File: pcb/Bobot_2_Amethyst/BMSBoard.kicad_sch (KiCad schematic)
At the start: 5 parts, among them J3 Conn_01x05_Socket, J4 Conn_01x04_Socket, J7 Conn_01x02_Pin, U1 BQ25895RTW

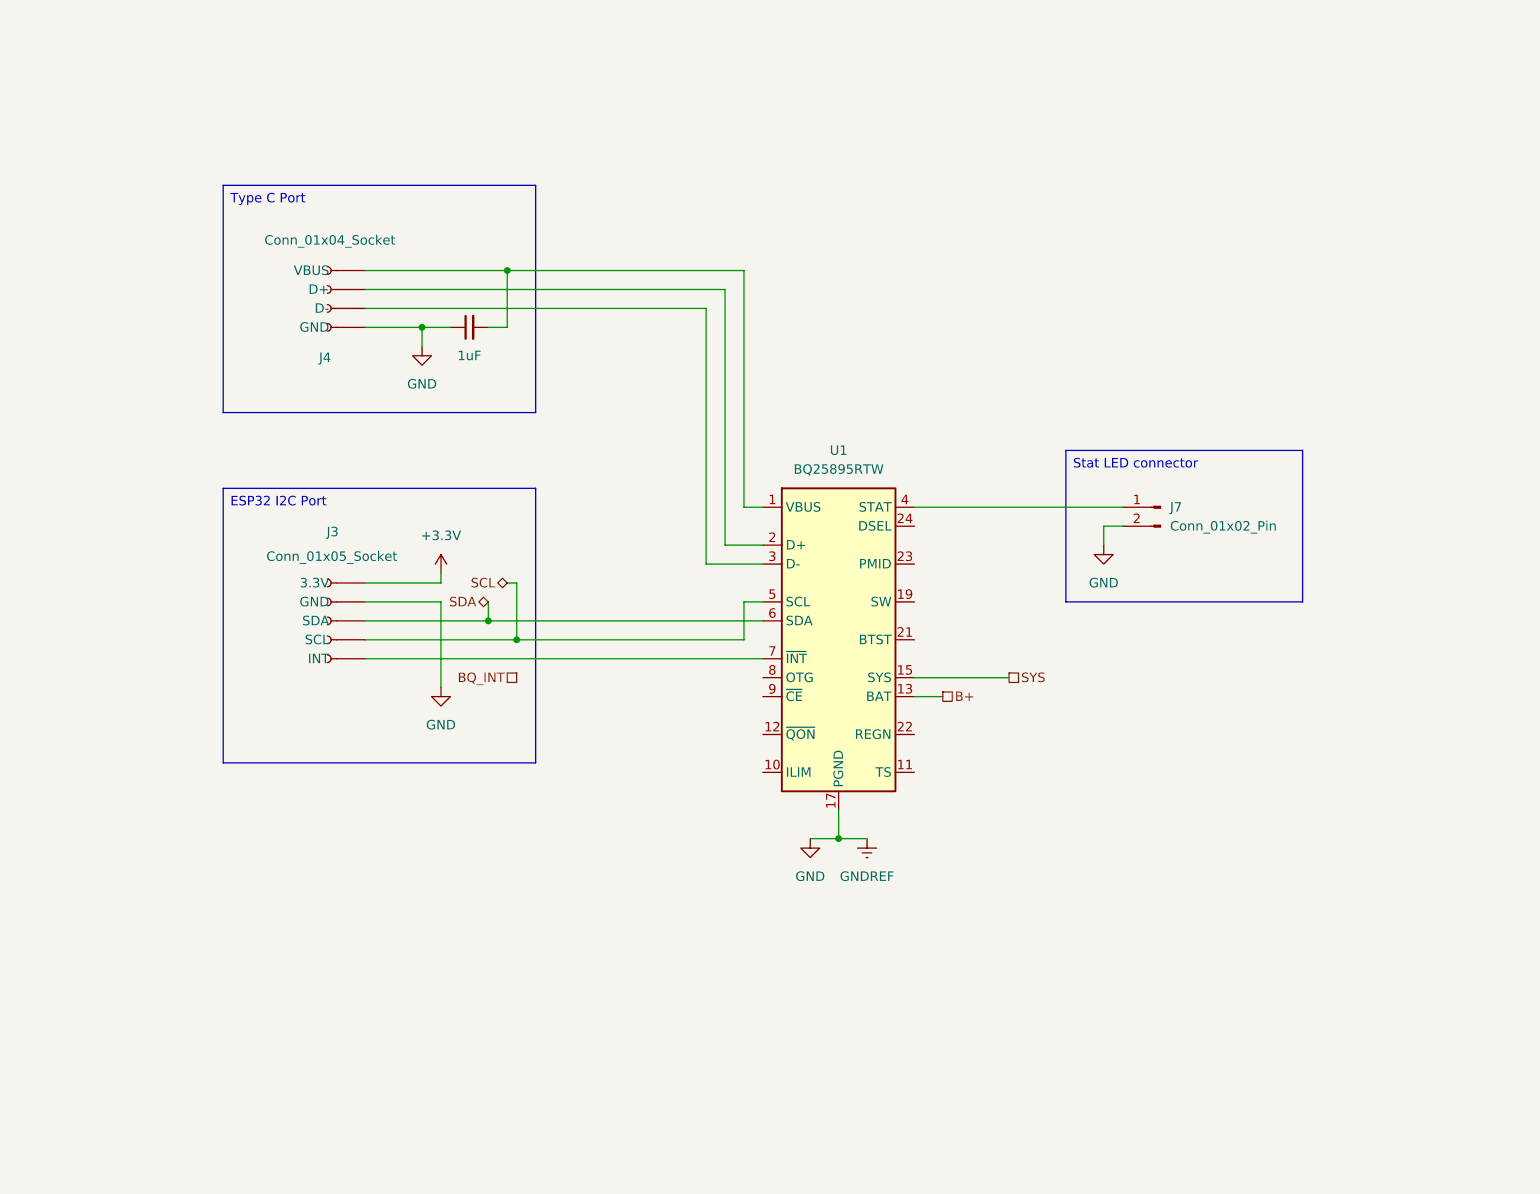
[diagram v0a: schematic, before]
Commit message: pcb: add battery and thermistor connection schematics
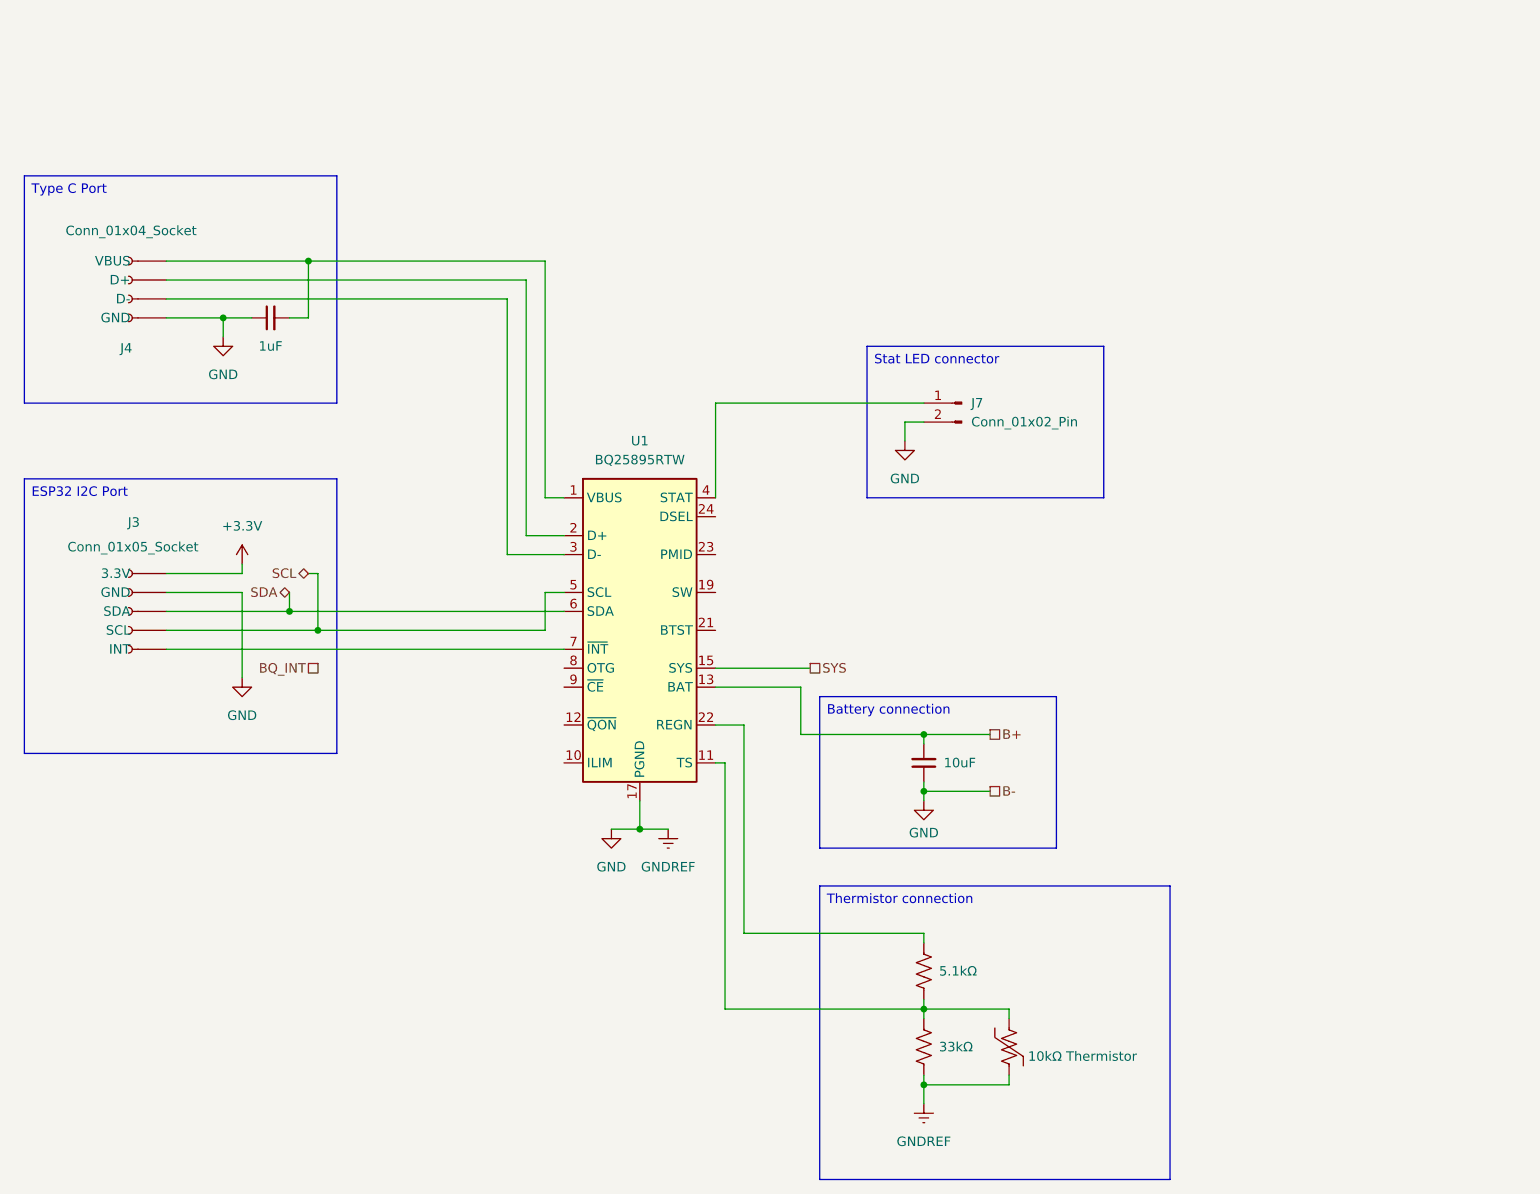
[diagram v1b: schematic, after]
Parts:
- added C2: 10uF, Capacitor_SMD:C_0603_1608Metric, symbol Device:C_Small
- added R3: 33kΩ, Resistor_SMD:R_0201_0603Metric, symbol Device:R_US
- added R4: 5.1kΩ, Resistor_SMD:R_0201_0603Metric, symbol Device:R_US
- added TH1: 10kΩ Thermistor, TerminalBlock:TerminalBlock_MaiXu_MX126-5.0-02P_1x02_P5.00mm, symbol Device:Thermistor_US
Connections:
- net B+: now also C2.2
- net GND: now also C2.1, R3.2, TH1.2
- net at U1.11 (TS): now also R3.1, R4.2, TH1.1
- net at U1.22 (REGN): now also R4.1
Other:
- moved on the sheet: J3, J4, J7, U1

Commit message: pcb: complete BMS board schematic
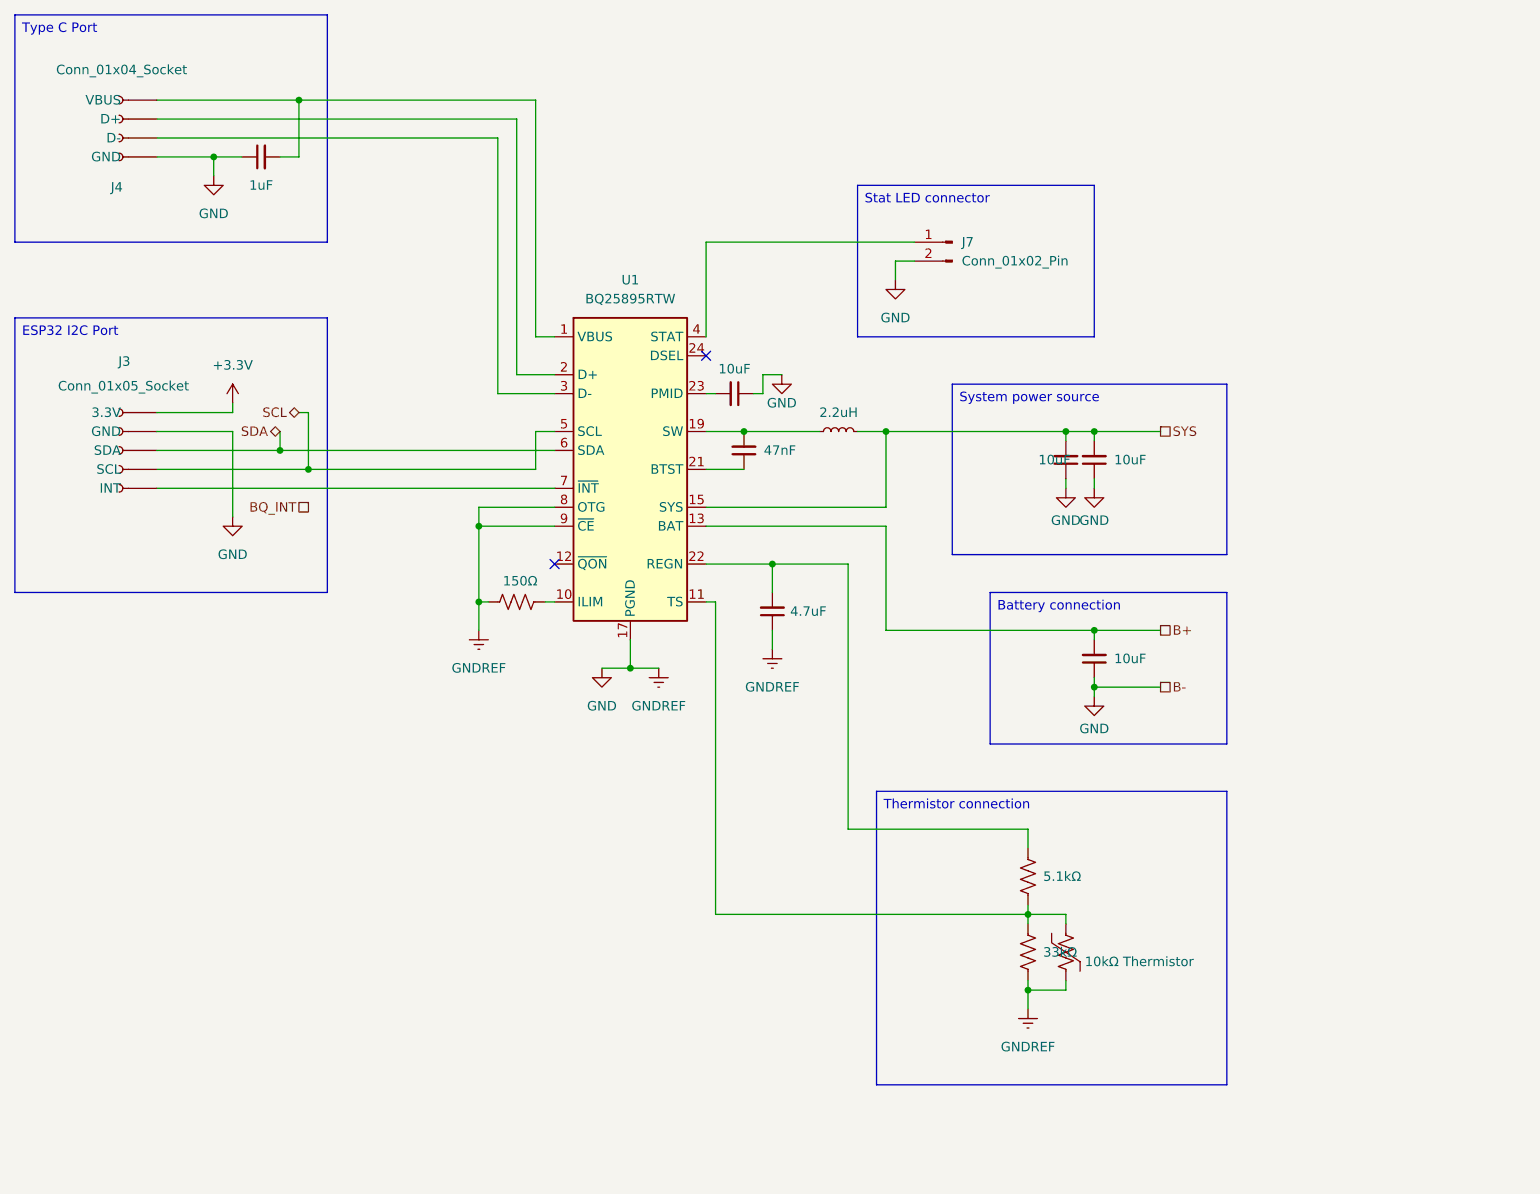
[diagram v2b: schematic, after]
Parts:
- added C3: 47nF, Capacitor_SMD:C_0805_2012Metric_Pad1.18x1.45mm_HandSolder, symbol Device:C_Small
- added C4: 4.7uF, Capacitor_SMD:C_0805_2012Metric_Pad1.18x1.45mm_HandSolder, symbol Device:C_Small
- added C5, C6, C7: 10uF, Capacitor_SMD:C_0805_2012Metric_Pad1.18x1.45mm_HandSolder, symbol Device:C_Small
- added L1: 2.2uH, Inductor_SMD:L_Chilisin_BMRF00101040, symbol Device:L_Small
- added R5: 150Ω, Resistor_SMD:R_0201_0603Metric, symbol Device:R_US
- C1, C2: footprint Capacitor_SMD:C_0603_1608Metric -> Capacitor_SMD:C_0805_2012Metric_Pad1.18x1.45mm_HandSolder
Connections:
- net GND: now also U1.8 (OTG), U1.9 (~{CE}), C4.1, C5.1, C6.1, C7.1, R5.1
- net SYS: now also C5.2, C6.2, L1.2
- net at R4.1, U1.22 (REGN): now also C4.2
- net at U1.10 (ILIM): now also R5.2
- net at U1.19 (SW), U1.20 (SW): now also C3.2, L1.1
- net at U1.21 (BTST): now also C3.1
- net at U1.23 (PMID): now also C7.2
- no-connect marks 0 -> 2
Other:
- moved on the sheet: J3, J4, J7, U1

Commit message: pcb: add buttons board schematics except I2C address
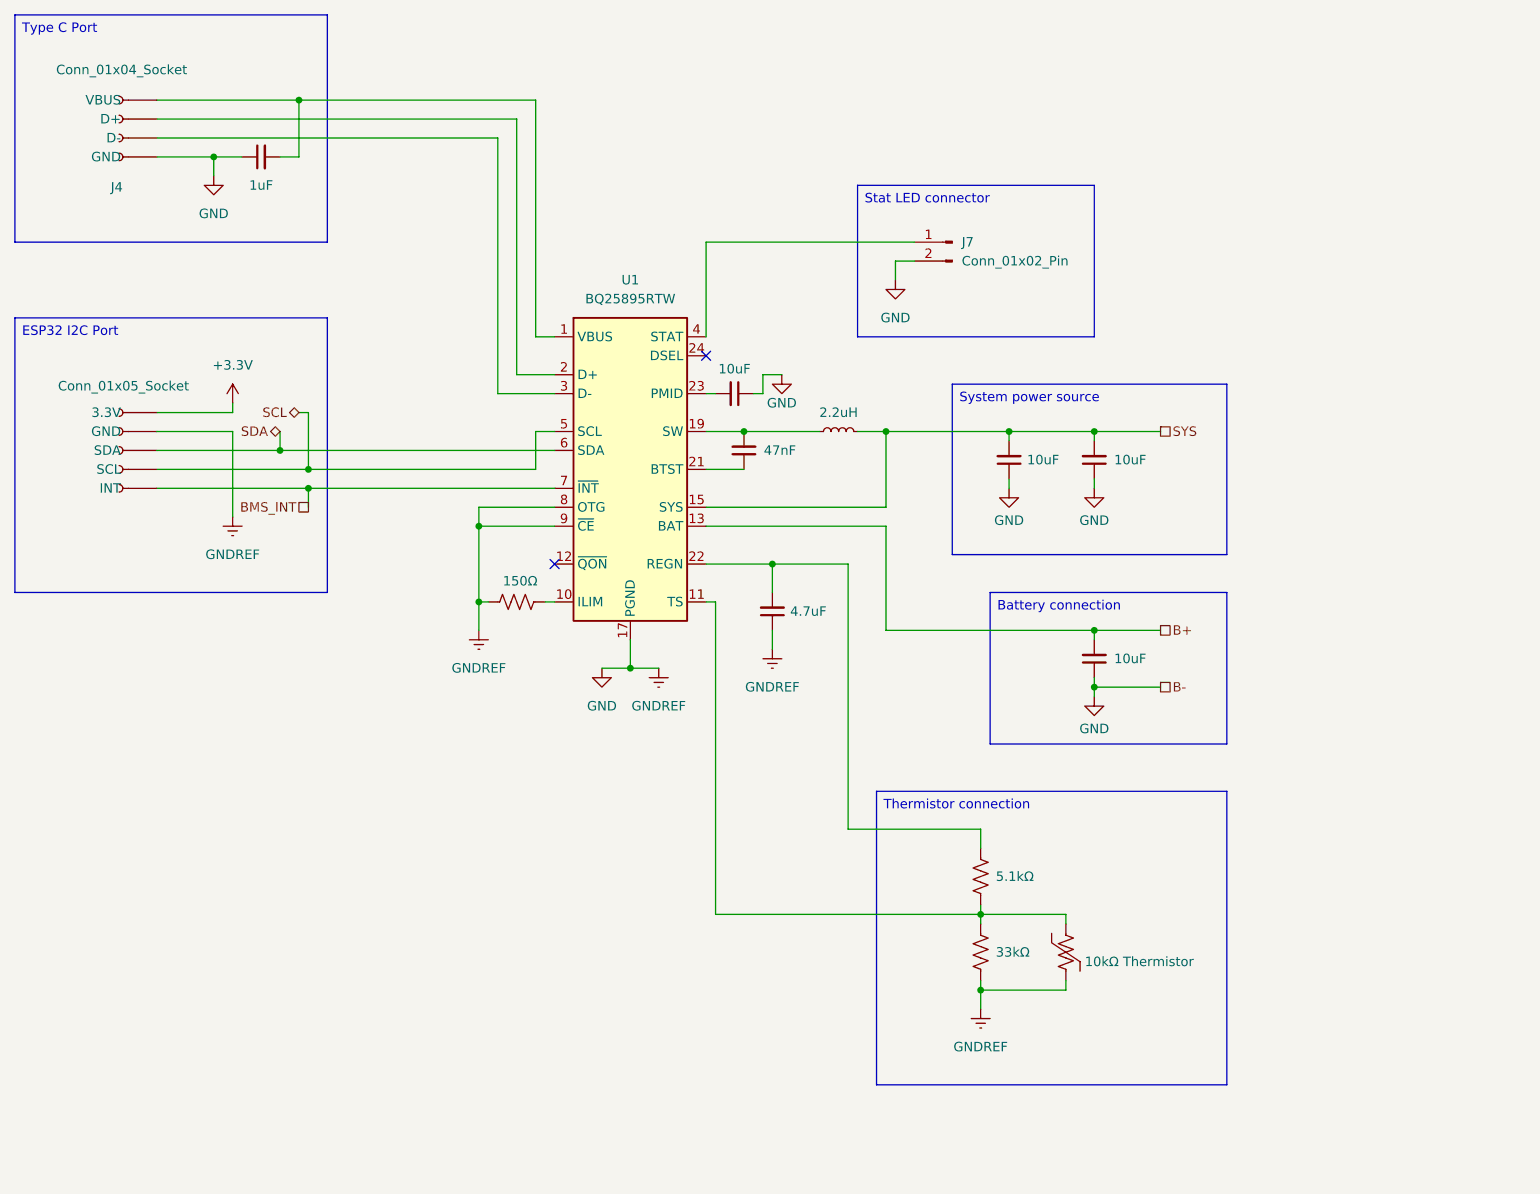
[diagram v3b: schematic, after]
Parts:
- R3, R4, R5: footprint Resistor_SMD:R_0201_0603Metric -> Resistor_SMD:R_0805_2012Metric_Pad1.20x1.40mm_HandSolder
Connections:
- net BMS_INT: now reaches J3.5 (INT), U1.7 (~{INT})

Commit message: pcb: add touch sensor board
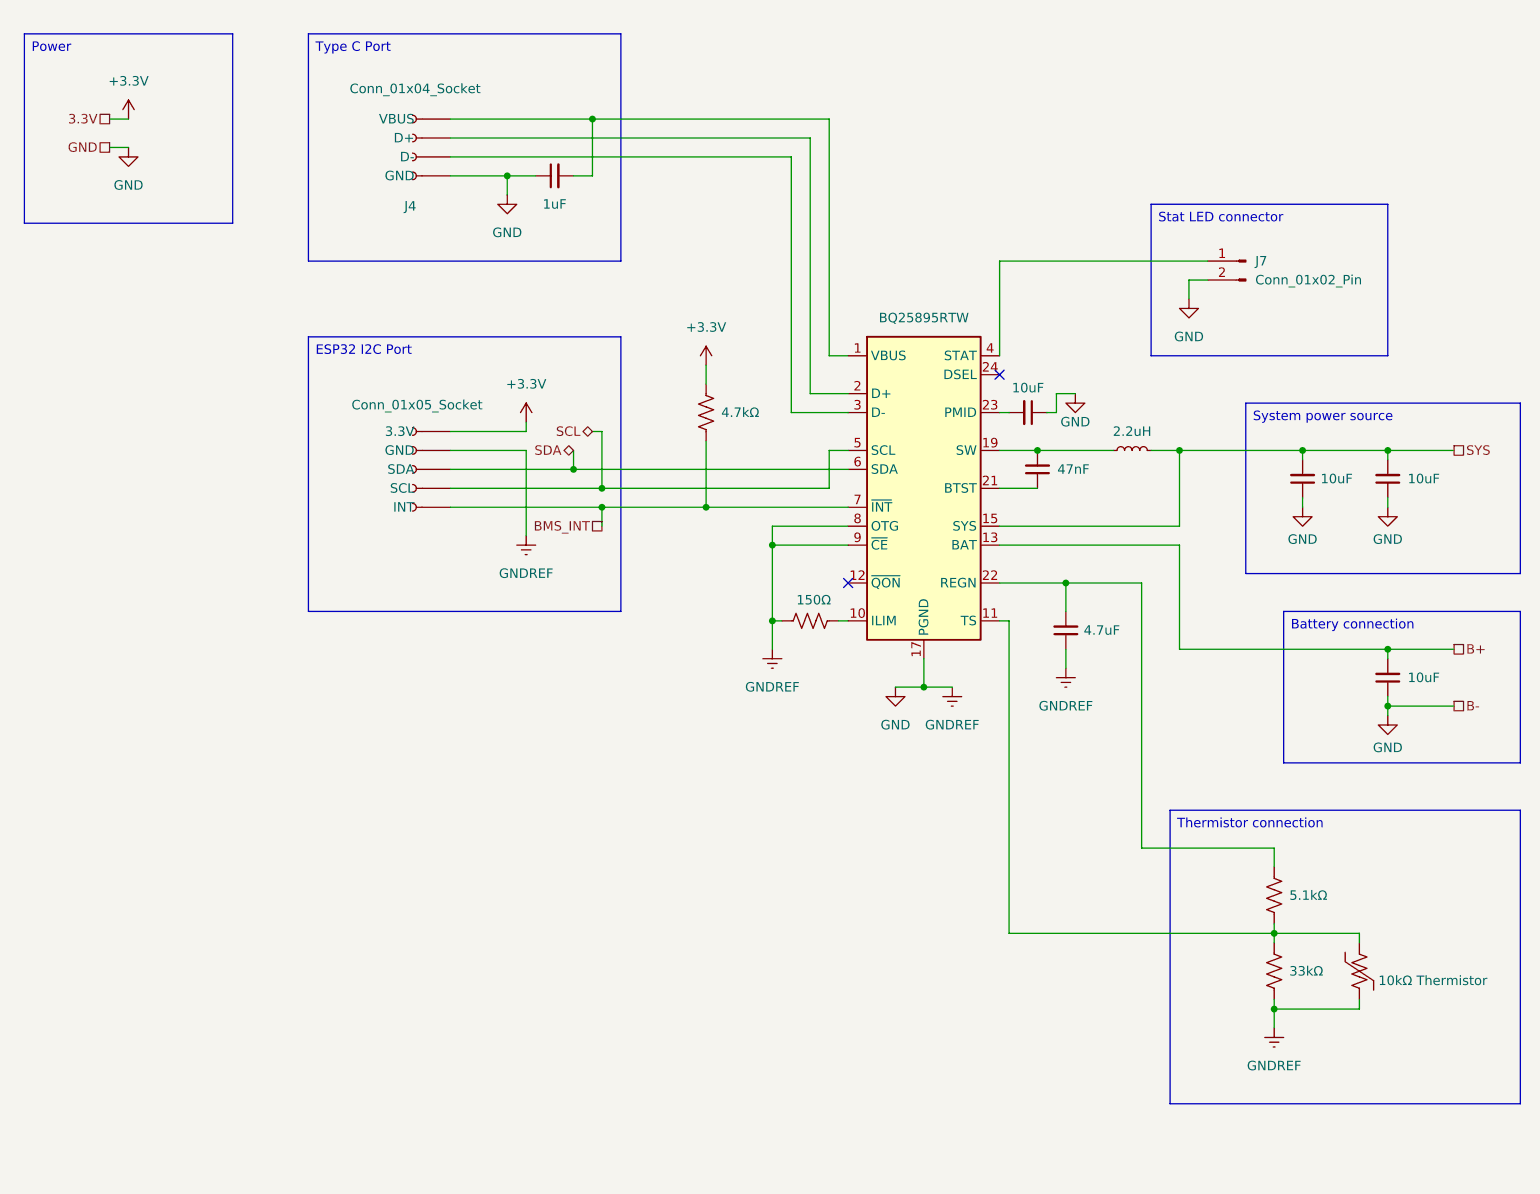
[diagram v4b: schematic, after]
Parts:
- added R25: 4.7kΩ, Resistor_SMD:R_0805_2012Metric_Pad1.20x1.40mm_HandSolder, symbol Device:R_US
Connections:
- net +3.3V: now also R25.1
- net BMS_INT: now also R25.2
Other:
- title: (none) -> BMS Board with BQ25895RTW
- moved on the sheet: J4, J7
